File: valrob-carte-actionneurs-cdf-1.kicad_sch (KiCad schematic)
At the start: 61 parts, among them J10 Conn_01x04_Pin, J2 Conn_01x02, J3 USB_C_Receptacle_USB2.0_14P, J4 Conn_01x02, M1 Motor_Servo, SW1 SW_Push, SW2 SW_Push, U2 SN65HVD230, U3 LDL212PV33R, U5 ESP32-S3FN8, Y1 48M

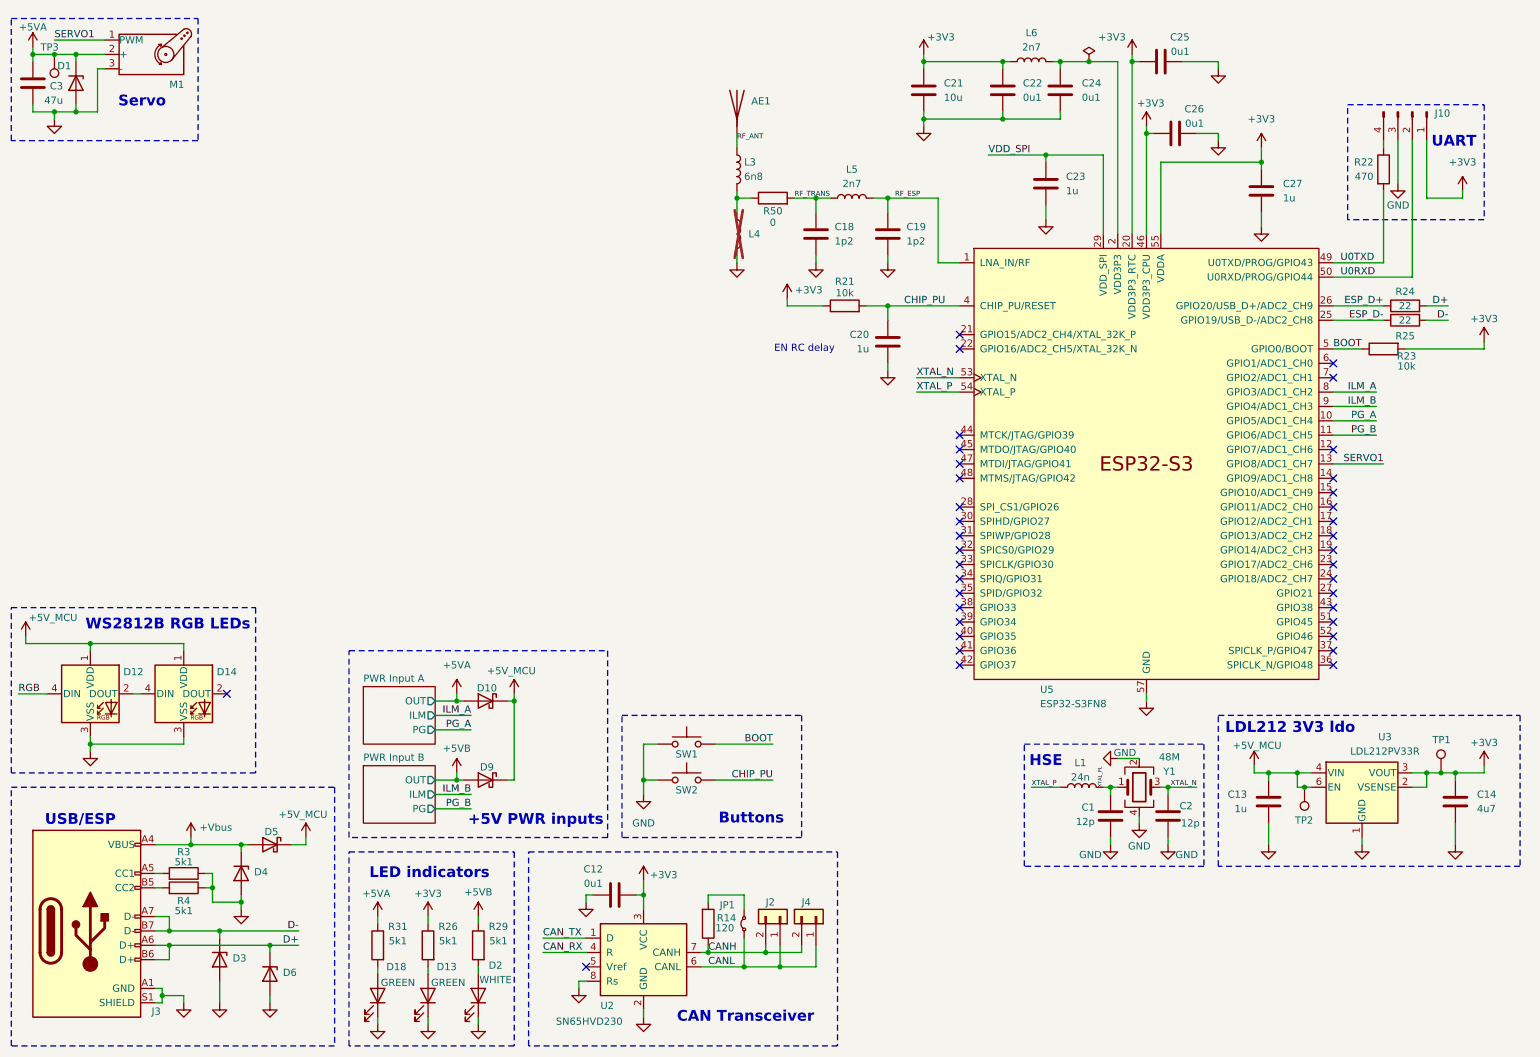
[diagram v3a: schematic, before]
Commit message: schem: add 14 servo channels
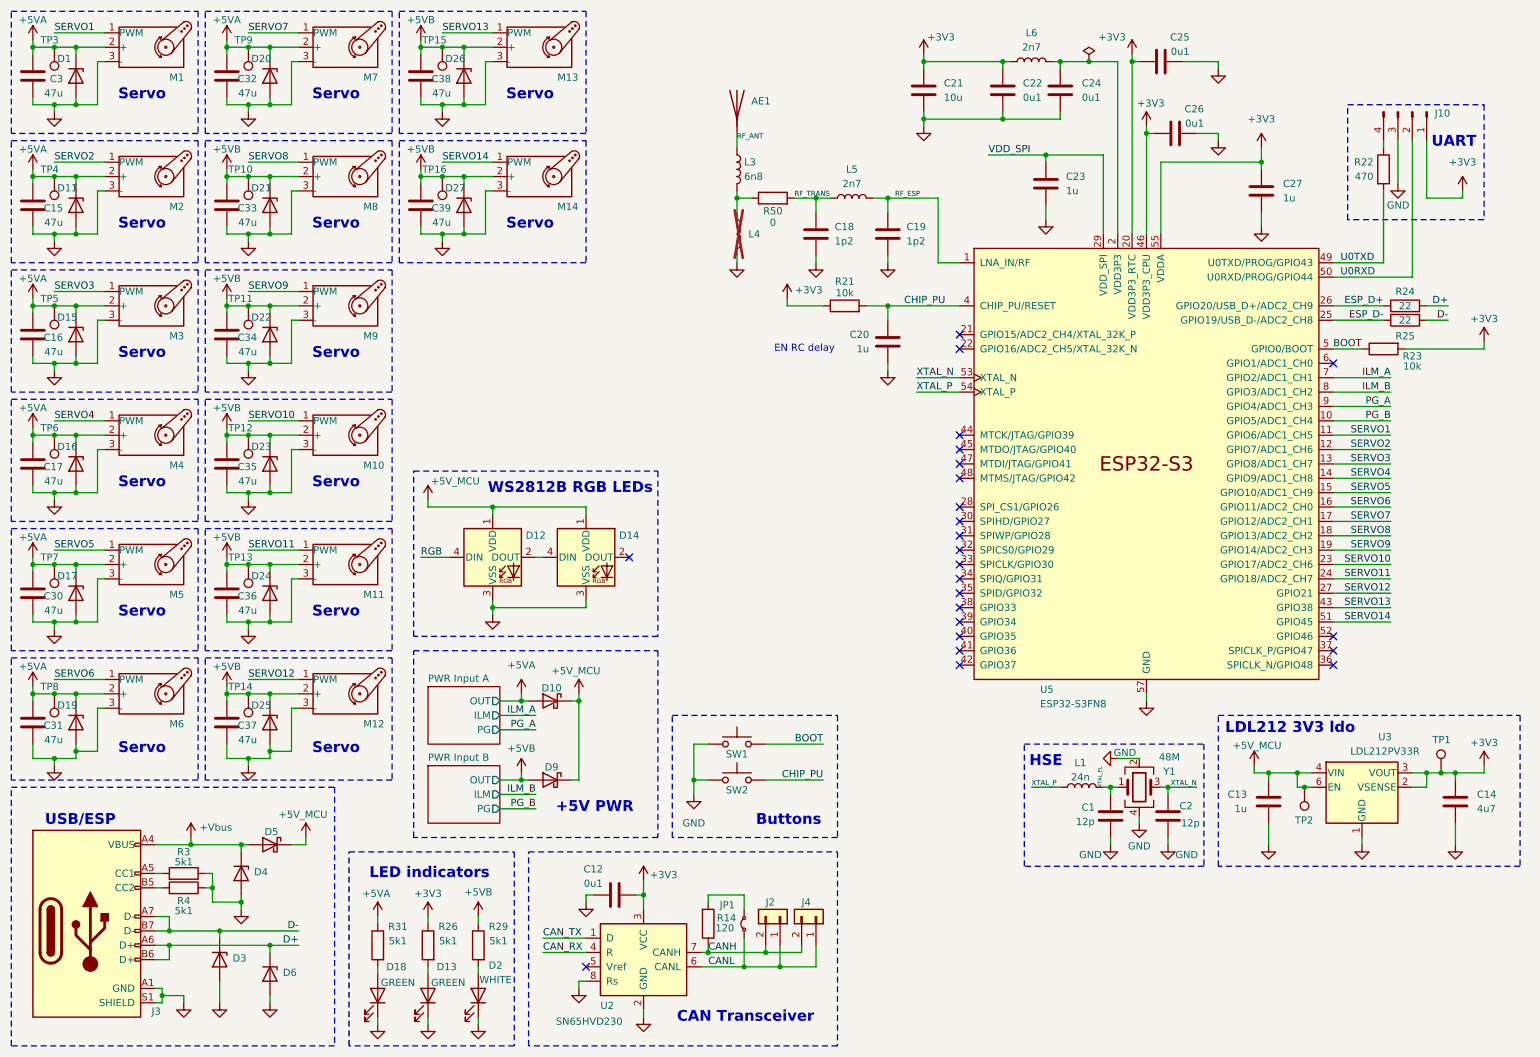
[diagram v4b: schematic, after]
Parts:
- added C15, C16, C17, C30, C31, C32, C33, C34, C35, C36, C37, C38, C39: 47u, Capacitor_SMD:C_1206_3216Metric, symbol Device:C
- added D11, D15, D16, D17, D19, D20, D21, D22, D23, D24, D25, D26, D27: H5VU10U, GLCS:Diode_DFN1006, symbol GLCS:H5VU10U
- added M10, M11, M12, M13, M14, M2, M3, M4, M5, M6, M7, M8, M9: Motor_Servo, Connector_PinHeader_2.54mm:PinHeader_1x03_P2.54mm_Vertical, symbol Motor:Motor_Servo
- added TP10, TP11, TP12, TP13, TP14, TP15, TP16, TP4, TP5, TP6, TP7, TP8, TP9: TestPoint, TestPoint:TestPoint_Pad_D2.0mm, symbol Connector:TestPoint
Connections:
- net +5VA: now also C15.1, C16.1, C17.1, C30.1, C31.1, C32.1, D11.1 (K), D15.1 (K), D16.1 (K), D17.1 (K), D19.1 (K), D20.1 (K), M2.2 (+), M3.2 (+), M4.2 (+), M5.2 (+), M6.2 (+), M7.2 (+), TP4.1, TP5.1, TP6.1, TP7.1, TP8.1, TP9.1
- net +5VB: now also C33.1, C34.1, C35.1, C36.1, C37.1, C38.1, C39.1, D21.1 (K), D22.1 (K), D23.1 (K), D24.1 (K), D25.1 (K), D26.1 (K), D27.1 (K), M10.2 (+), M11.2 (+), M12.2 (+), M13.2 (+), M14.2 (+), M8.2 (+), M9.2 (+), TP10.1, TP11.1, TP12.1, TP13.1, TP14.1, TP15.1, TP16.1
- net GND: now also C15.2, C16.2, C17.2, C30.2, C31.2, C32.2, C33.2, C34.2, C35.2, C36.2, C37.2, C38.2, C39.2, D11.2 (A), D15.2 (A), D16.2 (A), D17.2 (A), D19.2 (A), D20.2 (A), D21.2 (A), D22.2 (A), D23.2 (A), D24.2 (A), D25.2 (A), D26.2 (A), D27.2 (A), M10.3 (-), M11.3 (-), M12.3 (-), M13.3 (-), M14.3 (-), M2.3 (-), M3.3 (-), M4.3 (-), M5.3 (-), M6.3 (-), M7.3 (-), M8.3 (-), M9.3 (-)
- net ILM_A: now also U5.7 (GPIO2/ADC1_CH1); no longer U5.8 (GPIO3/ADC1_CH2)
- net ILM_B: now also U5.8 (GPIO3/ADC1_CH2); no longer U5.9 (GPIO4/ADC1_CH3)
- net PG_A: now also U5.9 (GPIO4/ADC1_CH3); no longer U5.10 (GPIO5/ADC1_CH4)
- net PG_B: now also U5.10 (GPIO5/ADC1_CH4); no longer U5.11 (GPIO6/ADC1_CH5)
- net SERVO1: now also U5.11 (GPIO6/ADC1_CH5); no longer U5.13 (GPIO8/ADC1_CH7)
- net SERVO2: now reaches U5.12 (GPIO7/ADC1_CH6)
- net SERVO2: now also M2.1 (PWM)
- net SERVO4: now reaches U5.14 (GPIO9/ADC1_CH8)
- net SERVO4: now also M4.1 (PWM)
- net SERVO5: now reaches U5.15 (GPIO10/ADC1_CH9)
- net SERVO5: now also M5.1 (PWM)
- net SERVO6: now reaches U5.16 (GPIO11/ADC2_CH0)
- net SERVO6: now also M6.1 (PWM)
- net SERVO7: now reaches U5.17 (GPIO12/ADC2_CH1)
- net SERVO7: now also M7.1 (PWM)
- net SERVO8: now reaches U5.18 (GPIO13/ADC2_CH2)
- net SERVO8: now also M8.1 (PWM)
- net SERVO9: now reaches U5.19 (GPIO14/ADC2_CH3)
- net SERVO9: now also M9.1 (PWM)
- net SERVO10: now reaches U5.23 (GPIO17/ADC2_CH6)
- net SERVO10: now also M10.1 (PWM)
- net SERVO11: now reaches U5.24 (GPIO18/ADC2_CH7)
- net SERVO11: now also M11.1 (PWM)
- net SERVO12: now reaches U5.27 (GPIO21)
- net SERVO12: now also M12.1 (PWM)
- net SERVO13: now reaches U5.43 (GPIO38)
- net SERVO13: now also M13.1 (PWM)
- net SERVO14: now reaches U5.51 (GPIO45)
- net SERVO14: now also M14.1 (PWM)
- new net SERVO3: M3.1 (PWM), U5.13 (GPIO8/ADC1_CH7)
- no-connect marks 37 -> 24
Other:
- note added: "+5V PWR"
- note removed: "+5V PWR inputs"
- moved on the sheet: C3, D1, D10, D12, D14, D9, M1, SW1, SW2, TP3

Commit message: schem: run and fix ERC
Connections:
- net CAN_RX: now also U5.45 (MTDO/JTAG/GPIO40)
- net CAN_TX: now also U5.44 (MTCK/JTAG/GPIO39)
- net RGB: now also U5.6 (GPIO1/ADC1_CH0)
- no-connect marks 24 -> 21
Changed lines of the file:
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@@
 	)
 	(junction
+		(at 66.04 160.02)
+		(diameter 0)
+		(color 0 0 0 0)
+	)
+	(junction
 		(at 19.05 64.77)
 		(diameter 0)
@@
 	)
 	(junction
+		(at 44.45 186.69)
+		(diameter 0)
+		(color 0 0 0 0)
+	)
+	(junction
 		(at 22.86 19.05)
 		(diameter 0)
@@
 	)
 	(no_connect
-		(at 248.92 74.93)
-	)
-	(no_connect
 		(at 182.88 110.49)
 	)
@@
 	)
 	(no_connect
-		(at 182.88 90.17)
-	)
-	(no_connect
 		(at 182.88 72.39)
 	)
 	(no_connect
-		(at 182.88 87.63)
-	)
-	(no_connect
 		(at 182.88 123.19)
 	)
@@
 	(wire
 		(pts
+			(xy 175.26 87.63) (xy 182.88 87.63)
+		)
+		(stroke
+			(width 0)
+			(type default)
+		)
+	)
+	(wire
+		(pts
 			(xy 57.15 74.93) (xy 60.96 74.93)
 		)
@@
 	(wire
 		(pts
-			(xy 41.91 186.69) (xy 45.72 186.69)
+			(xy 41.91 186.69) (xy 44.45 186.69)
 		)
 		(stroke
@@
 	(wire
 		(pts
+			(xy 44.45 186.69) (xy 45.72 186.69)
+		)
+		(stroke
+			(width 0)
+			(type default)
+		)
+	)
+	(wire
+		(pts
 			(xy 242.57 147.32) (xy 237.49 147.32)
 		)
@@
 	(wire
 		(pts
+			(xy 175.26 90.17) (xy 182.88 90.17)
+		)
+		(stroke
+			(width 0)
+			(type default)
+		)
+	)
+	(wire
+		(pts
 			(xy 195.58 149.86) (xy 200.66 149.86)
 		)
@@
 	(wire
 		(pts
-			(xy 67.31 160.02) (xy 64.77 160.02)
+			(xy 67.31 160.02) (xy 66.04 160.02)
 		)
 		(stroke
@@
 	(wire
 		(pts
+			(xy 248.92 74.93) (xy 254 74.93)
+		)
+		(stroke
+			(width 0)
+			(type default)
+		)
+	)
+	(wire
+		(pts
 			(xy 22.86 85.09) (xy 31.75 85.09)
 		)
@@
 	(wire
 		(pts
+			(xy 66.04 160.02) (xy 64.77 160.02)
+		)
+		(stroke
+			(width 0)
+			(type default)
+		)
+	)
+	(wire
+		(pts
 			(xy 57.15 146.05) (xy 57.15 144.78)
 		)
@@
 		)
 	)
+	(label "RGB"
+		(at 254 74.93 180)
+		(effects
+			(font
+				(size 1.27 1.27)
+			)
+			(justify right bottom)
+		)
+	)
 	(label "RF_ANT"
 		(at 143.51 35.56 0)
@@
 		)
 	)
+	(label "CAN_TX"
+		(at 175.26 87.63 0)
+		(effects
+			(font
+				(size 1.27 1.27)
+			)
+			(justify left bottom)
+		)
+	)
 	(label "XTAL_N"
 		(at 175.26 77.47 0)
@@
 		)
 	)
+	(label "CAN_RX"
+		(at 175.26 90.17 0)
+		(effects
+			(font
+				(size 1.27 1.27)
+			)
+			(justify left bottom)
+		)
+	)
 	(symbol
 		(lib_id "Connector:USB_C_Receptacle_USB2.0_14P")
@@
 	)
 	(symbol
+		(lib_id "power:PWR_FLAG")
+		(at 44.45 186.69 0)
+		(unit 1)
+		(exclude_from_sim no)
+		(in_bom yes)
+		(on_board yes)
+		(dnp no)
+		(fields_autoplaced yes)
+		(property "Reference" "#FLG04"
+			(at 44.45 184.785 0)
+			(effects
+				(font
+					(size 1.27 1.27)
+				)
+				(hide yes)
+			)
+		)
+		(property "Value" "PWR_FLAG"
+			(at 44.45 181.61 0)
+			(effects
+				(font
+					(size 1.27 1.27)
+				)
+				(hide yes)
+			)
+		)
+		(property "Footprint" ""
+			(at 44.45 186.69 0)
+			(effects
+				(font
+					(size 1.27 1.27)
+				)
+				(hide yes)
+			)
+		)
+		(property "Datasheet" "~"
+			(at 44.45 186.69 0)
+			(effects
+				(font
+					(size 1.27 1.27)
+				)
+				(hide yes)
+			)
+		)
+		(property "Description" "Special symbol for telling ERC where power comes from"
+			(at 44.45 186.69 0)
+			(effects
+				(font
+					(size 1.27 1.27)
+				)
+				(hide yes)
+			)
+		)
+		(pin "1"
+		)
+		(instances
+			(project "valrob-carte-actionneurs-cdf-1"
+				(path "/6d04427e-e45e-4b7f-8323-501f87acc543"
+					(reference "#FLG04")
+					(unit 1)
+				)
+			)
+		)
+	)
+	(symbol
 		(lib_id "Motor:Motor_Servo")
 		(at 107.95 41.91 0)
@@
 					(unit 1)
 				)
+			)
+		)
+	)
+	(symbol
+		(lib_id "power:PWR_FLAG")
+		(at 66.04 160.02 180)
+		(unit 1)
+		(exclude_from_sim no)
+		(in_bom yes)
+		(on_board yes)
+		(dnp no)
+		(fields_autoplaced yes)
+		(property "Reference" "#FLG01"
+			(at 66.04 161.925 0)
+			(effects
+				(font
+					(size 1.27 1.27)
+				)
+				(hide yes)
+			)
+		)
+		(property "Value" "PWR_FLAG"
+			(at 66.04 165.1 0)
+			(effects
+				(font
+					(size 1.27 1.27)
+				)
+				(hide yes)
+			)
+		)
+		(property "Footprint" ""
+			(at 66.04 160.02 0)
+			(effects
+				(font
+					(size 1.27 1.27)
+				)
+				(hide yes)
+			)
+		)
+		(property "Datasheet" "~"
+			(at 66.04 160.02 0)
+			(effects
+				(font
+					(size 1.27 1.27)
+				)
+				(hide yes)
+			)
+		)
+		(property "Description" "Special symbol for telling ERC where power comes from"
+			(at 66.04 160.02 0)
+			(effects
+				(font
+					(size 1.27 1.27)
+				)
+				(hide yes)
+			)
+		)
+		(pin "1"
+		)
+		(instances
+			(project ""
+				(path "/6d04427e-e45e-4b7f-8323-501f87acc543"
+					(reference "#FLG01")
+					(unit 1)
+				)

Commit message: schem: fix BOM
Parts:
- L5, L6: now in the parts list
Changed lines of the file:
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@@
 		(unit 1)
 		(exclude_from_sim no)
-		(in_bom no)
+		(in_bom yes)
 		(on_board yes)
 		(dnp no)
@@
 		(unit 1)
 		(exclude_from_sim no)
-		(in_bom no)
+		(in_bom yes)
 		(on_board yes)
 		(dnp no)

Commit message: schem: add sheet title
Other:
- company: (none) -> Valrobotik
- title: (none) -> Carte actionneurs CDF 1
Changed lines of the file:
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@@
 	(generator_version "9.0")
 	(paper "A4")
+	(title_block
+		(title "Carte actionneurs CDF 1")
+		(date "2026-02-18")
+		(rev "01")
+		(company "Valrobotik")
+	)
 	(rectangle
 		(start 132.08 137.16)

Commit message: schem: reannotate
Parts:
- renumbered C3 to C1, C35 to C10, C36 to C11, C37 to C12, C38 to C13, C39 to C14, C12 to C15, C18 to C16, C19 to C17, C20 to C18, C21 to C19, C15 to C2, C22 to C20, C23 to C21, C24 to C22, C1 to C23, C25 to C24, C2 to C25, C13 to C28, C14 to C29, C16 to C3, C17 to C4, C30 to C5, C31 to C6, C32 to C7, C33 to C8, C34 to C9, D21 to D10, D22 to D11, D23 to D12, D24 to D13, D25 to D14, D5 to D15, D6 to D16, D18 to D17, D13 to D18, D26 to D19, D11 to D2, D27 to D20, D2 to D21, D12 to D22, D10 to D23, D9 to D24, D14 to D25, D15 to D3, D16 to D4, D17 to D5, D19 to D6, D3 to D7, D4 to D8, D20 to D9, J3 to J1, J4 to J3, J10 to J4, L3 to L1, L4 to L2, L5 to L3, L6 to L4, L1 to L5, R3 to R1, R23 to R10, R24 to R11, R25 to R12, R4 to R2, R31 to R3, R26 to R4, R29 to R5, R14 to R6, R50 to R7, R21 to R8, R22 to R9, TP3 to TP1, TP12 to TP10, TP13 to TP11, TP14 to TP12, TP15 to TP13, TP16 to TP14, TP2 to TP15, TP1 to TP16, TP4 to TP2, TP5 to TP3, TP6 to TP4, TP7 to TP5, TP8 to TP6, TP9 to TP7, TP10 to TP8, TP11 to TP9, U2 to U1, U5 to U2
